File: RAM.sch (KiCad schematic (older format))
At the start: 1 part, among them U1 xc7a50tftg256

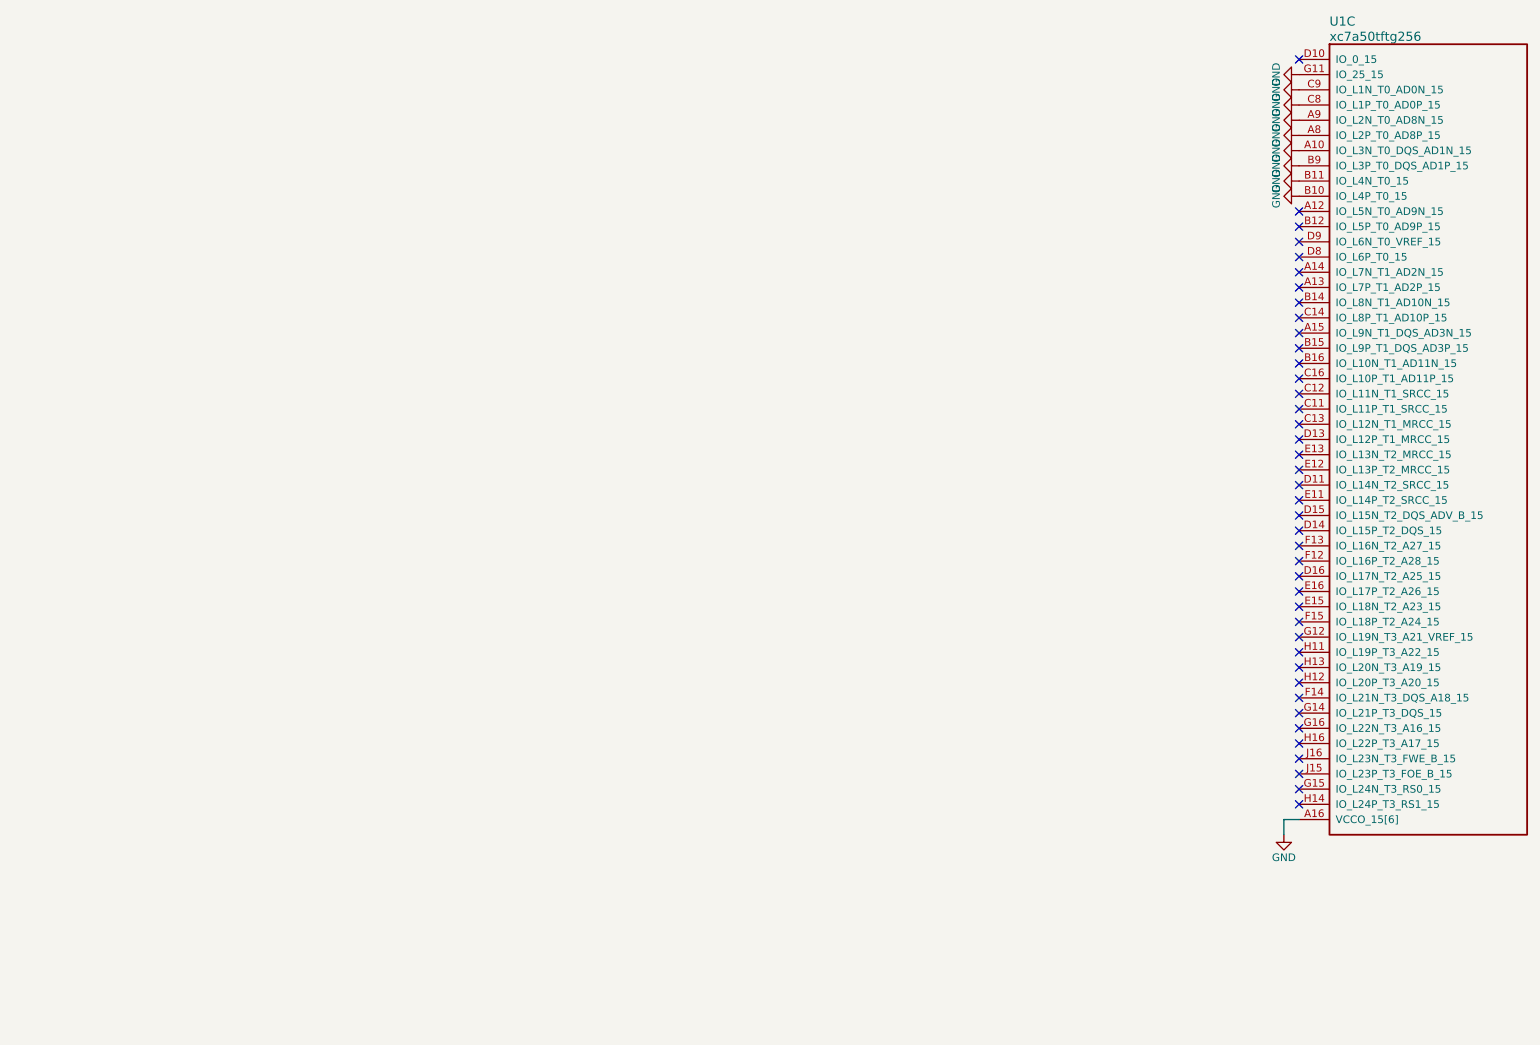
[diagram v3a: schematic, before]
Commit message: added and length-matched DDR2 ram, compliant to Xilinx MIG
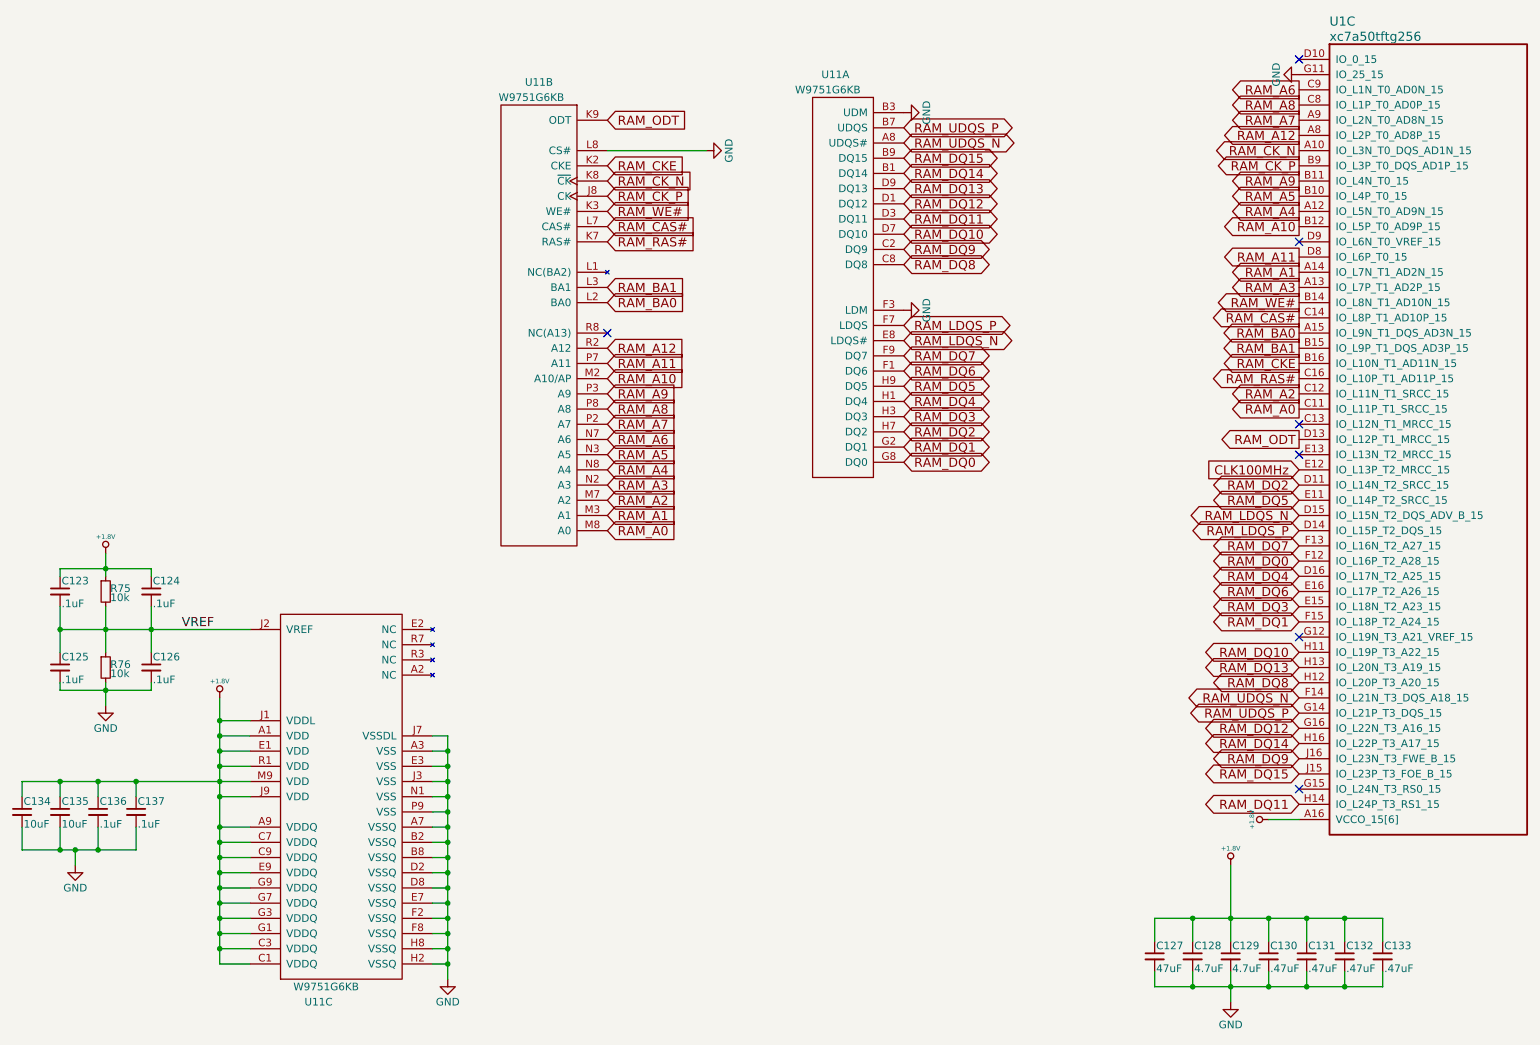
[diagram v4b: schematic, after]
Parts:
- added C123, C124, C125, C126, C136, C137: .1uF, Capacitors_SMD:C_0603, symbol C_Small
- added C127: 47uF, Capacitors_SMD:C_1210, symbol C_Small
- added C128, C129: 4.7uF, Capacitors_SMD:C_0805, symbol C_Small
- added C130, C131, C132, C133: .47uF, Capacitors_SMD:C_0603, symbol C_Small
- added C134, C135: 10uF, Capacitors_SMD:C_0805, symbol C_Small
- added R75, R76: 10k, Resistors_SMD:R_0402, symbol R_Small
- added U11: W9751G6KB, DFTcustom:WBGA-84, symbol W9751G6KB
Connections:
- net GND: now also C125.2, C126.2, C127.2, C128.2, C129.2, C130.2, C131.2, C132.2, C133.2, C134.2, C135.2, C136.2, C137.2, R76.2, U11.A3 (VSS), U11.A7 (VSSQ), U11.B2 (VSSQ), U11.B3 (UDM), U11.B8 (VSSQ), U11.D2 (VSSQ), U11.D8 (VSSQ), U11.E3 (VSS), U11.E7 (VSSQ), U11.F2 (VSSQ), U11.F3 (LDM), U11.F8 (VSSQ), U11.H2 (VSSQ), U11.H8 (VSSQ), U11.J3 (VSS), U11.J7 (VSSDL), U11.L8 (CS#), U11.N1 (VSS), U11.P9 (VSS); no longer U1.A10 (IO_L3N_T0_DQS_AD1N_15), U1.A16 (VCCO_15[6]), U1.A8 (IO_L2P_T0_AD8P_15), U1.A9 (IO_L2N_T0_AD8N_15), U1.B10 (IO_L4P_T0_15), U1.B11 (IO_L4N_T0_15), U1.B13 (VCCO_15[6]), U1.B9 (IO_L3P_T0_DQS_AD1P_15), U1.C10 (VCCO_15[6]), U1.C8 (IO_L1P_T0_AD0P_15), U1.C9 (IO_L1N_T0_AD0N_15), U1.E14 (VCCO_15[6]), U1.H15 (VCCO_15[6]), U1.J12 (VCCO_15[6])
- net RAM_A4: now reaches U1.A12 (IO_L5N_T0_AD9N_15)
- net RAM_A4: now also U11.N8 (A4)
- net RAM_A3: now reaches U1.A13 (IO_L7P_T1_AD2P_15)
- net RAM_A3: now also U11.N2 (A3)
- net RAM_A1: now reaches U1.A14 (IO_L7N_T1_AD2N_15)
- net RAM_A1: now also U11.M3 (A1)
- net RAM_BA0: now reaches U1.A15 (IO_L9N_T1_DQS_AD3N_15)
- net RAM_BA0: now also U11.L2 (BA0)
- net RAM_A10: now reaches U1.B12 (IO_L5P_T0_AD9P_15)
- net RAM_A10: now also U11.M2 (A10/AP)
- net RAM_WE#: now reaches U1.B14 (IO_L8N_T1_AD10N_15)
- net RAM_WE#: now also U11.K3 (WE#)
- net RAM_BA1: now reaches U1.B15 (IO_L9P_T1_DQS_AD3P_15)
- net RAM_BA1: now also U11.L3 (BA1)
- net RAM_CKE: now reaches U1.B16 (IO_L10N_T1_AD11N_15)
- net RAM_CKE: now also U11.K2 (CKE)
- net RAM_A0: now reaches U1.C11 (IO_L11P_T1_SRCC_15)
- net RAM_A0: now also U11.M8 (A0)
- net RAM_A2: now reaches U1.C12 (IO_L11N_T1_SRCC_15)
- net RAM_A2: now also U11.M7 (A2)
- net RAM_CAS#: now reaches U1.C14 (IO_L8P_T1_AD10P_15)
- net RAM_CAS#: now also U11.L7 (CAS#)
- net RAM_RAS#: now reaches U1.C16 (IO_L10P_T1_AD11P_15)
- net RAM_RAS#: now also U11.K7 (RAS#)
- net RAM_DQ2: now reaches U1.D11 (IO_L14N_T2_SRCC_15)
- net RAM_DQ2: now also U11.H7 (DQ2)
- net RAM_ODT: now reaches U1.D13 (IO_L12P_T1_MRCC_15)
- net RAM_ODT: now also U11.K9 (ODT)
- net RAM_LDQS_P: now reaches U1.D14 (IO_L15P_T2_DQS_15)
- net RAM_LDQS_P: now also U11.F7 (LDQS)
- net RAM_LDQS_N: now reaches U1.D15 (IO_L15N_T2_DQS_ADV_B_15)
- net RAM_LDQS_N: now also U11.E8 (LDQS#)
- net RAM_DQ4: now reaches U1.D16 (IO_L17N_T2_A25_15)
- net RAM_DQ4: now also U11.H1 (DQ4)
- net RAM_A11: now reaches U1.D8 (IO_L6P_T0_15)
- net RAM_A11: now also U11.P7 (A11)
- net RAM_DQ5: now reaches U1.E11 (IO_L14P_T2_SRCC_15)
- net RAM_DQ5: now also U11.H9 (DQ5)
- net CLK100MHz: now reaches U1.E12 (IO_L13P_T2_MRCC_15)
- net RAM_DQ3: now reaches U1.E15 (IO_L18N_T2_A23_15)
- net RAM_DQ3: now also U11.H3 (DQ3)
- net RAM_DQ6: now reaches U1.E16 (IO_L17P_T2_A26_15)
- net RAM_DQ6: now also U11.F1 (DQ6)
- net RAM_DQ0: now reaches U1.F12 (IO_L16P_T2_A28_15)
- net RAM_DQ0: now also U11.G8 (DQ0)
- net RAM_DQ7: now reaches U1.F13 (IO_L16N_T2_A27_15)
- net RAM_DQ7: now also U11.F9 (DQ7)
- net RAM_UDQS_N: now reaches U1.F14 (IO_L21N_T3_DQS_A18_15)
- net RAM_UDQS_N: now also U11.A8 (UDQS#)
- net RAM_DQ1: now reaches U1.F15 (IO_L18P_T2_A24_15)
- net RAM_DQ1: now also U11.G2 (DQ1)
- net RAM_UDQS_P: now reaches U1.G14 (IO_L21P_T3_DQS_15)
- net RAM_UDQS_P: now also U11.B7 (UDQS)
- net RAM_DQ12: now reaches U1.G16 (IO_L22N_T3_A16_15)
- net RAM_DQ12: now also U11.D1 (DQ12)
- net RAM_DQ10: now reaches U1.H11 (IO_L19P_T3_A22_15)
- net RAM_DQ10: now also U11.D7 (DQ10)
- net RAM_DQ8: now reaches U1.H12 (IO_L20P_T3_A20_15)
- net RAM_DQ8: now also U11.C8 (DQ8)
- net RAM_DQ13: now reaches U1.H13 (IO_L20N_T3_A19_15)
- net RAM_DQ13: now also U11.D9 (DQ13)
- net RAM_DQ11: now reaches U1.H14 (IO_L24P_T3_RS1_15)
- net RAM_DQ11: now also U11.D3 (DQ11)
- net RAM_DQ14: now reaches U1.H16 (IO_L22P_T3_A17_15)
- net RAM_DQ14: now also U11.B1 (DQ14)
- net RAM_DQ15: now reaches U1.J15 (IO_L23P_T3_FOE_B_15)
- net RAM_DQ15: now also U11.B9 (DQ15)
- net RAM_DQ9: now reaches U1.J16 (IO_L23N_T3_FWE_B_15)
- net RAM_DQ9: now also U11.C2 (DQ9)
- new net +1.8V: C123.1, C124.1, C127.1, C128.1, C129.1, C130.1, C131.1, C132.1, C133.1, C134.1, C135.1, C136.1, C137.1, R75.1, U1.A16 (VCCO_15[6]), U1.B13 (VCCO_15[6]), U1.C10 (VCCO_15[6]), U1.E14 (VCCO_15[6]), U1.H15 (VCCO_15[6]), U1.J12 (VCCO_15[6]), U11.A1 (VDD), U11.A9 (VDDQ), U11.C1 (VDDQ), U11.C3 (VDDQ), U11.C7 (VDDQ), U11.C9 (VDDQ), U11.E1 (VDD), U11.E9 (VDDQ), U11.G1 (VDDQ), U11.G3 (VDDQ), U11.G7 (VDDQ), U11.G9 (VDDQ), U11.J1 (VDDL), U11.J9 (VDD), U11.M9 (VDD), U11.R1 (VDD)
- new net RAM_A12: U1.A8 (IO_L2P_T0_AD8P_15), U11.R2 (A12)
- new net RAM_A5: U1.B10 (IO_L4P_T0_15), U11.N3 (A5)
- new net RAM_A6: U1.C9 (IO_L1N_T0_AD0N_15), U11.N7 (A6)
- new net RAM_A7: U1.A9 (IO_L2N_T0_AD8N_15), U11.P2 (A7)
- new net RAM_A8: U1.C8 (IO_L1P_T0_AD0P_15), U11.P8 (A8)
- new net RAM_A9: U1.B11 (IO_L4N_T0_15), U11.P3 (A9)
- new net RAM_CK_N: U1.A10 (IO_L3N_T0_DQS_AD1N_15), U11.K8 (~CK)
- new net RAM_CK_P: U1.B9 (IO_L3P_T0_DQS_AD1P_15), U11.J8 (CK)
- new net VREF: C123.2, C124.2, C125.1, C126.1, R75.2, R76.1, U11.J2 (VREF)
- no-connect marks 41 -> 7

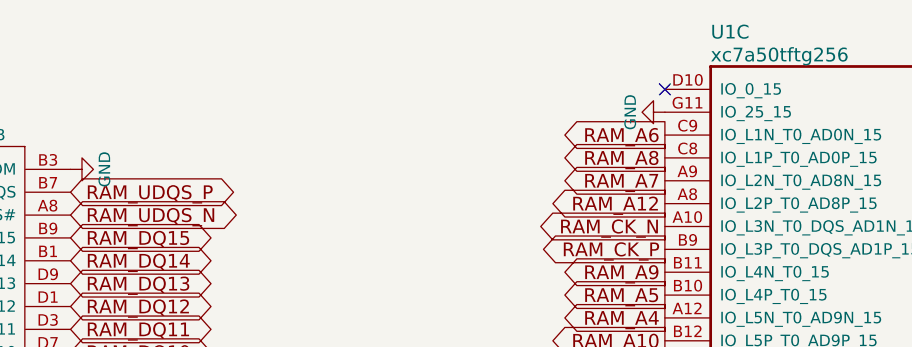
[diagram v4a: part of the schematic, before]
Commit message: all high speed busses added
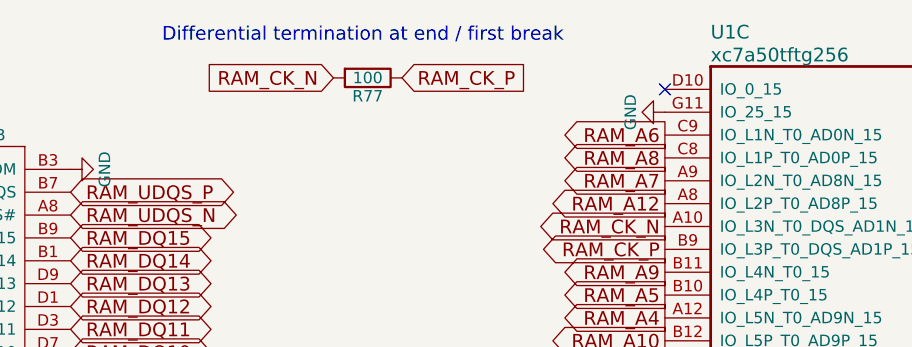
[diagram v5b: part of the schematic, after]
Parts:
- added R77: 100, Resistors_SMD:R_0402, symbol R
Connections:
- net RAM_CK_N: now also R77.2
- net RAM_CK_P: now also R77.1
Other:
- note added: "Differential termination at end / first break"
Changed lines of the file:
@@
 Text GLabel 6550 3700 2    60   BiDi ~ 0
 RAM_DQ0
-Text GLabel 4600 1850 2    60   Input ~ 0
-RAM_CK_N
-Text GLabel 4600 1950 2    60   Input ~ 0
-RAM_CK_P
 Text GLabel 6550 3600 2    60   BiDi ~ 0
 RAM_DQ1
@@
 Text GLabel 9150 3850 0    60   BiDi ~ 0
 RAM_DQ2
-Text GLabel 9150 1750 0    60   Output ~ 0
-RAM_CK_P
 Text GLabel 9150 3150 0    60   Output ~ 0
 RAM_RAS#
-Text GLabel 9150 1650 0    60   Output ~ 0
-RAM_CK_N
 Text GLabel 9150 3050 0    60   Output ~ 0
 RAM_CKE
@@
 Text GLabel 9150 1550 0    60   Output ~ 0
 RAM_A12
+Text GLabel 9150 1750 0    60   Output ~ 0
+RAM_CK_P
+Text GLabel 9150 1650 0    60   Output ~ 0
+RAM_CK_N
+Text GLabel 8000 1000 2    60   Input ~ 0
+RAM_CK_P
+Text GLabel 7700 1000 0    60   Input ~ 0
+RAM_CK_N
+Text GLabel 4600 1950 2    60   Input ~ 0
+RAM_CK_P
+Text GLabel 4600 1850 2    60   Input ~ 0
+RAM_CK_N
+$Comp
+L R R77
+U 1 1 5A7D1ACF
+P 7850 1000
+F 0 "R77" V 7930 1000 50  0000 C CNN
+F 1 "100" V 7850 1000 50  0000 C CNN
+F 2 "Resistors_SMD:R_0402" V 7780 1000 50  0001 C CNN
+F 3 "" H 7850 1000 50  0001 C CNN
+F 4 "Yageo" H 1750 -6050 50  0001 C CNN "MFR"
+F 5 "RC0402FR-07100RL" H 1750 -6050 50  0001 C CNN "MPN"
+F 6 "Digikey" H 1750 -6050 50  0001 C CNN "SPR"
+F 7 "311-100LRCT-ND" H 1750 -6050 50  0001 C CNN "SPN"
+F 8 "" H 1750 -6050 50  0001 C CNN "SPURL"
+	1    7850 1000
+	0    1    1    0
+$EndComp
+Text Notes 6950 850  0    60   ~ 0
+Differential termination at end / first break
 $EndSCHEMATC

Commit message: as submitted
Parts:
- C128, C129, C134, C135: footprint Capacitors_SMD:C_0805 -> Capacitors_SMD:C_0603
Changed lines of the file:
@@
 $EndComp
 $Comp
-L GND #PWR178
+L GND #PWR0169
 U 1 1 588278E2
 P 3550 7100
-F 0 "#PWR178" H 3550 6850 50  0001 C CNN
+F 0 "#PWR0169" H 3550 6850 50  0001 C CNN
 F 1 "GND" H 3550 6950 50  0000 C CNN
 F 2 "" H 3550 7100 50  0000 C CNN
@@
 $EndComp
 $Comp
-L +1.8V #PWR173
+L +1.8V #PWR0170
 U 1 1 58828168
 P 2050 5250
-F 0 "#PWR173" H 2050 5390 20  0001 C CNN
+F 0 "#PWR0170" H 2050 5390 20  0001 C CNN
 F 1 "+1.8V" H 2050 5360 30  0000 C CNN
 F 2 "" H 2050 5250 60  0001 C CNN
@@
 $EndComp
 $Comp
-L +1.8V #PWR175
+L +1.8V #PWR0171
 U 1 1 588297F8
 P 8950 6050
-F 0 "#PWR175" H 8950 6190 20  0001 C CNN
+F 0 "#PWR0171" H 8950 6190 20  0001 C CNN
 F 1 "+1.8V" H 8950 6160 30  0000 C CNN
 F 2 "" H 8950 6050 60  0001 C CNN
@@
 $EndComp
 $Comp
-L GND #PWR174
+L GND #PWR0172
 U 1 1 58829F20
 P 1300 5300
-F 0 "#PWR174" H 1300 5050 50  0001 C CNN
+F 0 "#PWR0172" H 1300 5050 50  0001 C CNN
 F 1 "GND" H 1300 5150 50  0000 C CNN
 F 2 "" H 1300 5300 50  0000 C CNN
@@
 $EndComp
 $Comp
-L +1.8V #PWR172
+L +1.8V #PWR0173
 U 1 1 5882A093
 P 1300 4300
-F 0 "#PWR172" H 1300 4440 20  0001 C CNN
+F 0 "#PWR0173" H 1300 4440 20  0001 C CNN
 F 1 "+1.8V" H 1300 4410 30  0000 C CNN
 F 2 "" H 1300 4300 60  0001 C CNN
@@
 F 0 "C135" H 1010 6070 50  0000 L CNN
 F 1 "10uF" H 1010 5920 50  0000 L CNN
-F 2 "Capacitors_SMD:C_0805" H 1000 6000 50  0001 C CNN
+F 2 "Capacitors_SMD:C_0603" H 1000 6000 50  0001 C CNN
 F 3 "" H 1000 6000 50  0001 C CNN
 F 4 "Murata" H 0   0   50  0001 C CNN "MFR"
@@
 F 0 "C134" H 760 6070 50  0000 L CNN
 F 1 "10uF" H 760 5920 50  0000 L CNN
-F 2 "Capacitors_SMD:C_0805" H 750 6000 50  0001 C CNN
+F 2 "Capacitors_SMD:C_0603" H 750 6000 50  0001 C CNN
 F 3 "" H 750 6000 50  0001 C CNN
 F 4 "Murata" H 0   0   50  0001 C CNN "MFR"
@@
 $EndComp
 $Comp
-L GND #PWR176
+L GND #PWR0174
 U 1 1 588352D5
 P 1100 6350
-F 0 "#PWR176" H 1100 6100 50  0001 C CNN
+F 0 "#PWR0174" H 1100 6100 50  0001 C CNN
 F 1 "GND" H 1100 6200 50  0000 C CNN
 F 2 "" H 1100 6350 50  0000 C CNN
@@
 F 0 "C128" H 8460 7020 50  0000 L CNN
 F 1 "4.7uF" H 8460 6870 50  0000 L CNN
-F 2 "Capacitors_SMD:C_0805" H 8450 6950 50  0001 C CNN
+F 2 "Capacitors_SMD:C_0603" H 8450 6950 50  0001 C CNN
 F 3 "" H 8450 6950 50  0001 C CNN
 F 4 "Murata" H 1300 1000 50  0001 C CNN "MFR"
@@
 F 0 "C129" H 8710 7020 50  0000 L CNN
 F 1 "4.7uF" H 8710 6870 50  0000 L CNN
-F 2 "Capacitors_SMD:C_0805" H 8700 6950 50  0001 C CNN
+F 2 "Capacitors_SMD:C_0603" H 8700 6950 50  0001 C CNN
 F 3 "" H 8700 6950 50  0001 C CNN
 F 4 "Murata" H 1300 1000 50  0001 C CNN "MFR"
@@
 $EndComp
 $Comp
-L GND #PWR179
+L GND #PWR0175
 U 1 1 5887E465
 P 8700 7250
-F 0 "#PWR179" H 8700 7000 50  0001 C CNN
+F 0 "#PWR0175" H 8700 7000 50  0001 C CNN
 F 1 "GND" H 8700 7100 50  0000 C CNN
 F 2 "" H 8700 7250 50  0000 C CNN
@@
 $EndComp
 $Comp
-L +1.8V #PWR177
+L +1.8V #PWR0176
 U 1 1 5887E495
 P 8700 6350
-F 0 "#PWR177" H 8700 6490 20  0001 C CNN
+F 0 "#PWR0176" H 8700 6490 20  0001 C CNN
 F 1 "+1.8V" H 8700 6460 30  0000 C CNN
 F 2 "" H 8700 6350 60  0001 C CNN
@@
 $EndComp
 $Comp
-L GND #PWR168
+L GND #PWR0177
 U 1 1 58945519
 P 9150 1150
-F 0 "#PWR168" H 9150 900 50  0001 C CNN
+F 0 "#PWR0177" H 9150 900 50  0001 C CNN
 F 1 "GND" H 9150 1000 50  0000 C CNN
 F 2 "" H 9150 1150 50  0000 C CNN
@@
 NoConn ~ 9150 3450
 $Comp
-L GND #PWR169
+L GND #PWR0178
 U 1 1 5A75637F
 P 6550 1400
-F 0 "#PWR169" H 6550 1150 50  0001 C CNN
+F 0 "#PWR0178" H 6550 1150 50  0001 C CNN
 F 1 "GND" H 6550 1250 50  0000 C CNN
 F 2 "" H 6550 1400 50  0000 C CNN
@@
 $EndComp
 $Comp
-L GND #PWR171
+L GND #PWR0179
 U 1 1 5A7563C9
 P 6550 2700
-F 0 "#PWR171" H 6550 2450 50  0001 C CNN
+F 0 "#PWR0179" H 6550 2450 50  0001 C CNN
 F 1 "GND" H 6550 2550 50  0000 C CNN
 F 2 "" H 6550 2700 50  0000 C CNN
@@
 CLK100MHz
 $Comp
-L GND #PWR170
+L GND #PWR0180
 U 1 1 5A7B46ED
 P 5250 1650
-F 0 "#PWR170" H 5250 1400 50  0001 C CNN
+F 0 "#PWR0180" H 5250 1400 50  0001 C CNN
 F 1 "GND" H 5250 1500 50  0000 C CNN
 F 2 "" H 5250 1650 50  0000 C CNN
